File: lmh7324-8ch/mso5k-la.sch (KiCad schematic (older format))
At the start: 10 parts, among them J101 out, J102 in, J103 3mm, J104 3mm, J105 3mm, J106 3mm

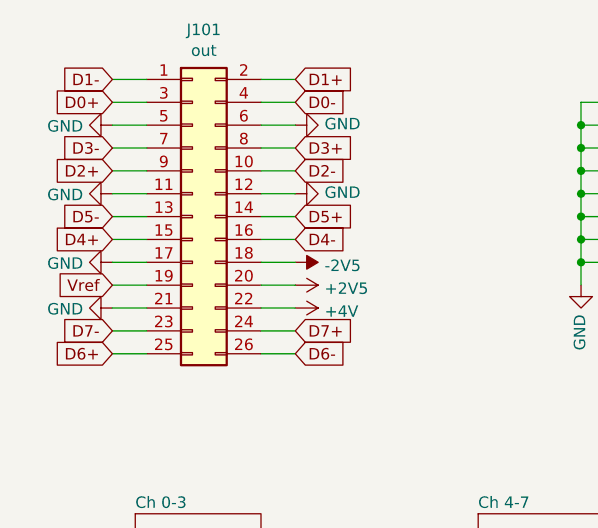
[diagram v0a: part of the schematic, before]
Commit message: Switched to an SMD 1.27 mm pitch header for the cable to the scope to get a thinner uplink ribbon
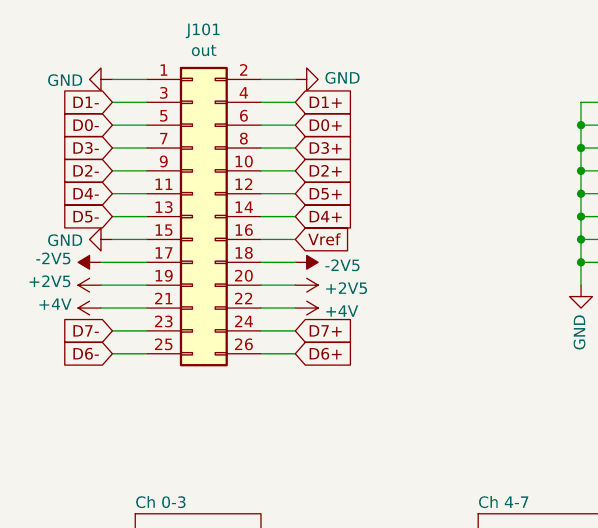
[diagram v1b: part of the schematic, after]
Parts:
- J101: footprint Connector_PinHeader_2.00mm:PinHeader_2x13_P2.00mm_Vertical -> Connector_PinHeader_1.27mm:PinHeader_2x13_P1.27mm_Vertical_SMD
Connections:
- net +2V5: now also J101.19 (Pin_19)
- net +4V: now also J101.21 (Pin_21)
- net -2V5: now also J101.17 (Pin_17)
- net D0+: now also J101.6 (Pin_6); no longer J101.3 (Pin_3)
- net D0-: now also J101.5 (Pin_5); no longer J101.4 (Pin_4)
- net D1+: now also J101.4 (Pin_4); no longer J101.2 (Pin_2)
- net D1-: now also J101.3 (Pin_3); no longer J101.1 (Pin_1)
- net D2+: now also J101.10 (Pin_10); no longer J101.9 (Pin_9)
- net D2-: now also J101.9 (Pin_9); no longer J101.10 (Pin_10)
- net D4+: now also J101.14 (Pin_14); no longer J101.15 (Pin_15)
- net D4-: now also J101.11 (Pin_11); no longer J101.16 (Pin_16)
- net D5+: now also J101.12 (Pin_12); no longer J101.14 (Pin_14)
- net D6+: now also J101.26 (Pin_26); no longer J101.25 (Pin_25)
- net D6-: now also J101.25 (Pin_25); no longer J101.26 (Pin_26)
- net GND: now also J101.1 (Pin_1), J101.15 (Pin_15), J101.2 (Pin_2); no longer J101.11 (Pin_11), J101.12 (Pin_12), J101.17 (Pin_17), J101.21 (Pin_21), J101.5 (Pin_5), J101.6 (Pin_6)
- net Vref: now also J101.16 (Pin_16); no longer J101.19 (Pin_19)
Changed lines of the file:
@@
 Comment4 ""
 $EndDescr
-$Comp
-L power:GND #PWR0106
-U 1 1 5C3F979B
-P 1600 1400
-F 0 "#PWR0106" H 1600 1150 50  0001 C CNN
-F 1 "GND" V 1605 1272 50  0000 R CNN
-F 2 "" H 1600 1400 50  0001 C CNN
-F 3 "" H 1600 1400 50  0001 C CNN
-	1    1600 1400
-	0    1    1    0
-$EndComp
 Text GLabel 2400 2300 2    50   Input ~ 0
 D7+
 Text GLabel 1600 2300 0    50   Input ~ 0
 D7-
-Text GLabel 1600 2400 0    50   Input ~ 0
+Text GLabel 2400 2400 2    50   Input ~ 0
 D6+
 $Comp
 L power:GND #PWR0109
 U 1 1 5C3F97D2
-P 2400 1400
-F 0 "#PWR0109" H 2400 1150 50  0001 C CNN
-F 1 "GND" V 2405 1272 50  0000 R CNN
-F 2 "" H 2400 1400 50  0001 C CNN
-F 3 "" H 2400 1400 50  0001 C CNN
-	1    2400 1400
-	0    -1   -1   0
-$EndComp
-Text GLabel 2400 2400 2    50   Input ~ 0
+P 2400 1200
+F 0 "#PWR0109" H 2400 950 50  0001 C CNN
+F 1 "GND" V 2405 1072 50  0000 R CNN
+F 2 "" H 2400 1200 50  0001 C CNN
+F 3 "" H 2400 1200 50  0001 C CNN
+	1    2400 1200
+	0    -1   -1   0
+$EndComp
+Text GLabel 1600 2400 0    50   Input ~ 0
 D6-
+Text GLabel 2400 1700 2    50   Input ~ 0
+D5+
 Text GLabel 2400 1800 2    50   Input ~ 0
-D5+
-Text GLabel 1600 1900 0    50   Input ~ 0
 D4+
 $Comp
 L power:GND #PWR0110
 U 1 1 5C3FA063
-P 1600 1700
-F 0 "#PWR0110" H 1600 1450 50  0001 C CNN
-F 1 "GND" V 1605 1572 50  0000 R CNN
-F 2 "" H 1600 1700 50  0001 C CNN
-F 3 "" H 1600 1700 50  0001 C CNN
-	1    1600 1700
+P 1600 1900
+F 0 "#PWR0110" H 1600 1650 50  0001 C CNN
+F 1 "GND" V 1605 1772 50  0000 R CNN
+F 2 "" H 1600 1900 50  0001 C CNN
+F 3 "" H 1600 1900 50  0001 C CNN
+	1    1600 1900
 	0    1    1    0
 $EndComp
 Text GLabel 1600 1800 0    50   Input ~ 0
 D5-
-Text GLabel 2400 1900 2    50   Input ~ 0
+Text GLabel 1600 1700 0    50   Input ~ 0
 D4-
 Text GLabel 2400 1500 2    50   Input ~ 0
 D3+
-Text GLabel 1600 1600 0    50   Input ~ 0
+Text GLabel 2400 1600 2    50   Input ~ 0
 D2+
 Text GLabel 1600 1500 0    50   Input ~ 0
 D3-
-Text GLabel 2400 1600 2    50   Input ~ 0
+Text GLabel 1600 1600 0    50   Input ~ 0
 D2-
-Text GLabel 2400 1200 2    50   Input ~ 0
+Text GLabel 2400 1300 2    50   Input ~ 0
 D1+
+Text GLabel 2400 1400 2    50   Input ~ 0
+D0+
 Text GLabel 1600 1300 0    50   Input ~ 0
-D0+
-Text GLabel 1600 1200 0    50   Input ~ 0
 D1-
-Text GLabel 2400 1300 2    50   Input ~ 0
+Text GLabel 1600 1400 0    50   Input ~ 0
 D0-
 $Comp
@@
 F 0 "J101" H 2000 2617 50  0000 C CNN
 F 1 "out" H 2000 2526 50  0000 C CNN
-F 2 "Connector_PinHeader_2.00mm:PinHeader_2x13_P2.00mm_Vertical" H 1950 1800 50  0001 C CNN
+F 2 "Connector_PinHeader_1.27mm:PinHeader_2x13_P1.27mm_Vertical_SMD" H 1950 1800 50  0001 C CNN
 F 3 "~" H 1950 1800 50  0001 C CNN
 	1    1950 1800
 	1    0    0    -1
 $EndComp
-Text GLabel 1600 2100 0    50   Input ~ 0
+Text GLabel 2400 1900 2    50   Input ~ 0
 Vref
 Wire Wire Line
+	1750 1300 1600 1300
+Wire Wire Line
 	1600 1400 1750 1400
 Wire Wire Line
-	1750 1200 1600 1200
-Wire Wire Line
-	1600 1300 1750 1300
-Wire Wire Line
 	1750 1500 1600 1500
 Wire Wire Line
 	1750 1600 1600 1600
 Wire Wire Line
+	1600 1700 1750 1700
+Wire Wire Line
 	1600 1800 1750 1800
 Wire Wire Line
-	1600 1900 1750 1900
-Wire Wire Line
 	1600 2300 1750 2300
 Wire Wire Line
 	1750 2400 1600 2400
 Wire Wire Line
-	1750 1700 1600 1700
-Wire Wire Line
-	1750 2100 1600 2100
+	1750 1900 1600 1900
+Wire Wire Line
+	2250 1900 2400 1900
 Wire Wire Line
 	2400 2200 2250 2200
@@
 	2400 2300 2250 2300
 Wire Wire Line
-	2250 1900 2400 1900
-Wire Wire Line
-	2400 1800 2250 1800
+	2250 1800 2400 1800
+Wire Wire Line
+	2400 1700 2250 1700
 Wire Wire Line
 	2250 1600 2400 1600
@@
 	2400 1500 2250 1500
 Wire Wire Line
-	2250 1300 2400 1300
-Wire Wire Line
-	2400 1200 2250 1200
-Wire Wire Line
 	2250 1400 2400 1400
+Wire Wire Line
+	2400 1300 2250 1300
+Wire Wire Line
+	2250 1200 2400 1200
 Text GLabel 1550 4250 0    50   Input ~ 0
 Vref
@@
 Text GLabel 6550 1500 1    50   Input ~ 0
 Vref
-$Comp
-L power:GND #PWR0102
-U 1 1 5C5F148B
-P 2400 1700
-F 0 "#PWR0102" H 2400 1450 50  0001 C CNN
-F 1 "GND" V 2405 1572 50  0000 R CNN
-F 2 "" H 2400 1700 50  0001 C CNN
-F 3 "" H 2400 1700 50  0001 C CNN
-	1    2400 1700
-	0    -1   -1   0
-$EndComp
-Wire Wire Line
-	2250 1700 2400 1700
-Wire Wire Line
-	1600 2000 1750 2000
-$Comp
-L power:GND #PWR0103
-U 1 1 5C600EBA
-P 1600 2000
-F 0 "#PWR0103" H 1600 1750 50  0001 C CNN
-F 1 "GND" V 1605 1872 50  0000 R CNN
-F 2 "" H 1600 2000 50  0001 C CNN
-F 3 "" H 1600 2000 50  0001 C CNN
-	1    1600 2000
-	0    1    1    0
-$EndComp
-$Comp
-L power:GND #PWR0105
-U 1 1 5C600ED1
-P 1600 2200
-F 0 "#PWR0105" H 1600 1950 50  0001 C CNN
-F 1 "GND" V 1605 2072 50  0000 R CNN
-F 2 "" H 1600 2200 50  0001 C CNN
-F 3 "" H 1600 2200 50  0001 C CNN
-	1    1600 2200
-	0    1    1    0
-$EndComp
-Wire Wire Line
-	1600 2200 1750 2200
 $Comp
 L Connector:Conn_01x01_Female J103
@@
 Wire Wire Line
 	5300 4000 5150 4000
+Wire Wire Line
+	1600 1200 1750 1200
+$Comp
+L power:GND #PWR0106
+U 1 1 5C3F979B
+P 1600 1200
+F 0 "#PWR0106" H 1600 950 50  0001 C CNN
+F 1 "GND" V 1605 1072 50  0000 R CNN
+F 2 "" H 1600 1200 50  0001 C CNN
+F 3 "" H 1600 1200 50  0001 C CNN
+	1    1600 1200
+	0    1    1    0
+$EndComp
+$Comp
+L power:-2V5 #PWR0102
+U 1 1 5C52E2DC
+P 1550 2000
+F 0 "#PWR0102" H 1550 2100 50  0001 C CNN
+F 1 "-2V5" V 1565 2128 50  0000 L CNN
+F 2 "" H 1550 2000 50  0001 C CNN
+F 3 "" H 1550 2000 50  0001 C CNN
+	1    1550 2000
+	0    -1   -1   0
+$EndComp
+$Comp
+L power:+2V5 #PWR0103
+U 1 1 5C52E30F
+P 1550 2100
+F 0 "#PWR0103" H 1550 1950 50  0001 C CNN
+F 1 "+2V5" V 1565 2228 50  0000 L CNN
+F 2 "" H 1550 2100 50  0001 C CNN
+F 3 "" H 1550 2100 50  0001 C CNN
+	1    1550 2100
+	0    -1   -1   0
+$EndComp
+$Comp
+L power:+4V #PWR0105
+U 1 1 5C52E342
+P 1550 2200
+F 0 "#PWR0105" H 1550 2050 50  0001 C CNN
+F 1 "+4V" V 1565 2328 50  0000 L CNN
+F 2 "" H 1550 2200 50  0001 C CNN
+F 3 "" H 1550 2200 50  0001 C CNN
+	1    1550 2200
+	0    -1   -1   0
+$EndComp
+Wire Wire Line
+	1550 2000 1750 2000
+Wire Wire Line
+	1750 2100 1550 2100
+Wire Wire Line
+	1550 2200 1750 2200
 $EndSCHEMATC

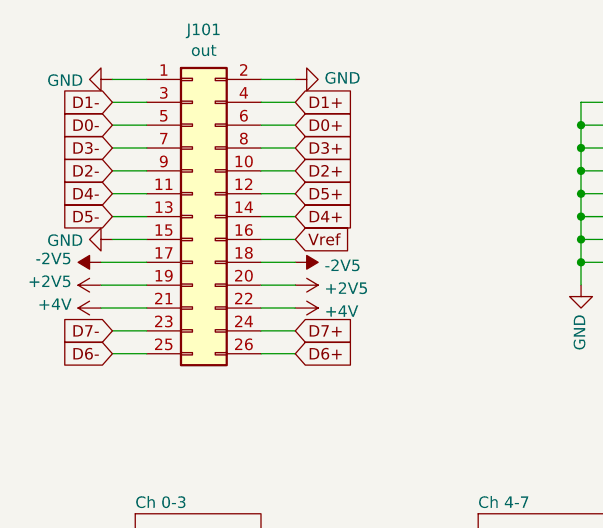
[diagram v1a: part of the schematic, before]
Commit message: Added breakout
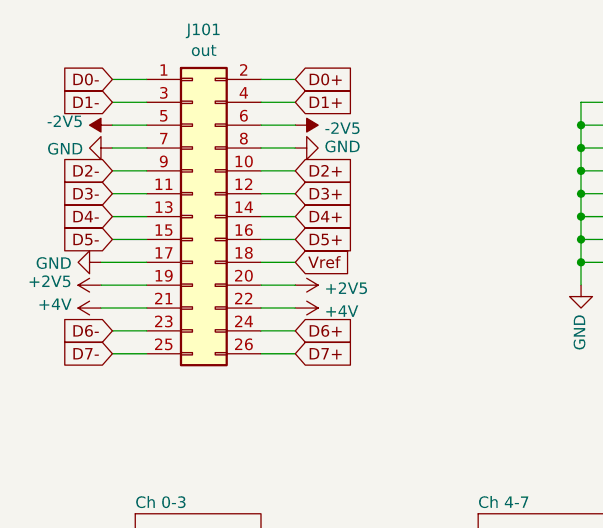
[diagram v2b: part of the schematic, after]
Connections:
- net -2V5: now also J101.5 (Pin_5), J101.6 (Pin_6); no longer J101.17 (Pin_17), J101.18 (Pin_18)
- net D0+: now also J101.2 (Pin_2); no longer J101.6 (Pin_6)
- net D0-: now also J101.1 (Pin_1); no longer J101.5 (Pin_5)
- net D3+: now also J101.12 (Pin_12); no longer J101.8 (Pin_8)
- net D3-: now also J101.11 (Pin_11); no longer J101.7 (Pin_7)
- net D4-: now also J101.13 (Pin_13); no longer J101.11 (Pin_11)
- net D5+: now also J101.16 (Pin_16); no longer J101.12 (Pin_12)
- net D5-: now also J101.15 (Pin_15); no longer J101.13 (Pin_13)
- net D6+: now also J101.24 (Pin_24); no longer J101.26 (Pin_26)
- net D6-: now also J101.23 (Pin_23); no longer J101.25 (Pin_25)
- net D7+: now also J101.26 (Pin_26); no longer J101.24 (Pin_24)
- net D7-: now also J101.25 (Pin_25); no longer J101.23 (Pin_23)
- net GND: now also J101.17 (Pin_17), J101.7 (Pin_7), J101.8 (Pin_8); no longer J101.1 (Pin_1), J101.15 (Pin_15), J101.2 (Pin_2)
- net Vref: now also J101.18 (Pin_18); no longer J101.16 (Pin_16)
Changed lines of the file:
@@
 Comment4 ""
 $EndDescr
+Text GLabel 2400 2400 2    50   Input ~ 0
+D7+
+Text GLabel 1600 2400 0    50   Input ~ 0
+D7-
 Text GLabel 2400 2300 2    50   Input ~ 0
-D7+
-Text GLabel 1600 2300 0    50   Input ~ 0
-D7-
-Text GLabel 2400 2400 2    50   Input ~ 0
 D6+
 $Comp
 L power:GND #PWR0109
 U 1 1 5C3F97D2
-P 2400 1200
-F 0 "#PWR0109" H 2400 950 50  0001 C CNN
-F 1 "GND" V 2405 1072 50  0000 R CNN
-F 2 "" H 2400 1200 50  0001 C CNN
-F 3 "" H 2400 1200 50  0001 C CNN
-	1    2400 1200
+P 2400 1500
+F 0 "#PWR0109" H 2400 1250 50  0001 C CNN
+F 1 "GND" V 2405 1372 50  0000 R CNN
+F 2 "" H 2400 1500 50  0001 C CNN
+F 3 "" H 2400 1500 50  0001 C CNN
+	1    2400 1500
 	0    -1   -1   0
 $EndComp
-Text GLabel 1600 2400 0    50   Input ~ 0
+Text GLabel 1600 2300 0    50   Input ~ 0
 D6-
-Text GLabel 2400 1700 2    50   Input ~ 0
+Text GLabel 2400 1900 2    50   Input ~ 0
 D5+
 Text GLabel 2400 1800 2    50   Input ~ 0
@@
 L power:GND #PWR0110
 U 1 1 5C3FA063
-P 1600 1900
-F 0 "#PWR0110" H 1600 1650 50  0001 C CNN
-F 1 "GND" V 1605 1772 50  0000 R CNN
-F 2 "" H 1600 1900 50  0001 C CNN
-F 3 "" H 1600 1900 50  0001 C CNN
-	1    1600 1900
+P 1550 2000
+F 0 "#PWR0110" H 1550 1750 50  0001 C CNN
+F 1 "GND" V 1555 1872 50  0000 R CNN
+F 2 "" H 1550 2000 50  0001 C CNN
+F 3 "" H 1550 2000 50  0001 C CNN
+	1    1550 2000
 	0    1    1    0
 $EndComp
+Text GLabel 1600 1900 0    50   Input ~ 0
+D5-
 Text GLabel 1600 1800 0    50   Input ~ 0
-D5-
-Text GLabel 1600 1700 0    50   Input ~ 0
 D4-
-Text GLabel 2400 1500 2    50   Input ~ 0
+Text GLabel 2400 1700 2    50   Input ~ 0
 D3+
 Text GLabel 2400 1600 2    50   Input ~ 0
 D2+
-Text GLabel 1600 1500 0    50   Input ~ 0
+Text GLabel 1600 1700 0    50   Input ~ 0
 D3-
 Text GLabel 1600 1600 0    50   Input ~ 0
@@
 Text GLabel 2400 1300 2    50   Input ~ 0
 D1+
-Text GLabel 2400 1400 2    50   Input ~ 0
+Text GLabel 2400 1200 2    50   Input ~ 0
 D0+
 Text GLabel 1600 1300 0    50   Input ~ 0
 D1-
-Text GLabel 1600 1400 0    50   Input ~ 0
+Text GLabel 1600 1200 0    50   Input ~ 0
 D0-
 $Comp
@@
 L power:-2V5 #PWR0101
 U 1 1 5C408E96
-P 2400 2000
-F 0 "#PWR0101" H 2400 2100 50  0001 C CNN
-F 1 "-2V5" V 2415 2128 50  0000 L CNN
-F 2 "" H 2400 2000 50  0001 C CNN
-F 3 "" H 2400 2000 50  0001 C CNN
-	1    2400 2000
+P 2400 1400
+F 0 "#PWR0101" H 2400 1500 50  0001 C CNN
+F 1 "-2V5" V 2415 1528 50  0000 L CNN
+F 2 "" H 2400 1400 50  0001 C CNN
+F 3 "" H 2400 1400 50  0001 C CNN
+	1    2400 1400
 	0    1    1    0
 $EndComp
@@
 	1    0    0    -1
 $EndComp
-Text GLabel 2400 1900 2    50   Input ~ 0
+Text GLabel 2400 2000 2    50   Input ~ 0
 Vref
 Wire Wire Line
@@
 L power:GND #PWR0106
 U 1 1 5C3F979B
-P 1600 1200
-F 0 "#PWR0106" H 1600 950 50  0001 C CNN
-F 1 "GND" V 1605 1072 50  0000 R CNN
-F 2 "" H 1600 1200 50  0001 C CNN
-F 3 "" H 1600 1200 50  0001 C CNN
-	1    1600 1200
+P 1600 1500
+F 0 "#PWR0106" H 1600 1250 50  0001 C CNN
+F 1 "GND" V 1605 1372 50  0000 R CNN
+F 2 "" H 1600 1500 50  0001 C CNN
+F 3 "" H 1600 1500 50  0001 C CNN
+	1    1600 1500
 	0    1    1    0
 $EndComp
@@
 L power:-2V5 #PWR0102
 U 1 1 5C52E2DC
-P 1550 2000
-F 0 "#PWR0102" H 1550 2100 50  0001 C CNN
-F 1 "-2V5" V 1565 2128 50  0000 L CNN
-F 2 "" H 1550 2000 50  0001 C CNN
-F 3 "" H 1550 2000 50  0001 C CNN
-	1    1550 2000
+P 1600 1400
+F 0 "#PWR0102" H 1600 1500 50  0001 C CNN
+F 1 "-2V5" V 1615 1528 50  0000 L CNN
+F 2 "" H 1600 1400 50  0001 C CNN
+F 3 "" H 1600 1400 50  0001 C CNN
+	1    1600 1400
 	0    -1   -1   0
 $EndComp

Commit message: Switched to 0805 on the pod for the large bulk caps
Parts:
- C101, C102, C103: footprint Capacitor_SMD:C_1206_3216Metric -> Capacitor_SMD:C_0805_2012Metric
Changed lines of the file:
@@
 F 0 "C101" H 5315 1846 50  0000 L CNN
 F 1 "10uF" H 5315 1755 50  0000 L CNN
-F 2 "Capacitor_SMD:C_1206_3216Metric" H 5238 1650 50  0001 C CNN
+F 2 "Capacitor_SMD:C_0805_2012Metric" H 5238 1650 50  0001 C CNN
 F 3 "~" H 5200 1800 50  0001 C CNN
 	1    5200 1800
@@
 F 0 "C102" H 5715 1846 50  0000 L CNN
 F 1 "10uF" H 5715 1755 50  0000 L CNN
-F 2 "Capacitor_SMD:C_1206_3216Metric" H 5638 1650 50  0001 C CNN
+F 2 "Capacitor_SMD:C_0805_2012Metric" H 5638 1650 50  0001 C CNN
 F 3 "~" H 5600 1800 50  0001 C CNN
 	1    5600 1800
@@
 F 0 "C103" H 6115 1846 50  0000 L CNN
 F 1 "10uF" H 6115 1755 50  0000 L CNN
-F 2 "Capacitor_SMD:C_1206_3216Metric" H 6038 1650 50  0001 C CNN
+F 2 "Capacitor_SMD:C_0805_2012Metric" H 6038 1650 50  0001 C CNN
 F 3 "~" H 6000 1800 50  0001 C CNN
 	1    6000 1800
